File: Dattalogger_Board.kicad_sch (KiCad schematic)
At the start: 25 parts, among them U1 24LC1025, U2 DS1337S_, U3 24LC1025, U4 ATMEGA328P-AU, Y1 32.768 KHz, Y2 16 MHz

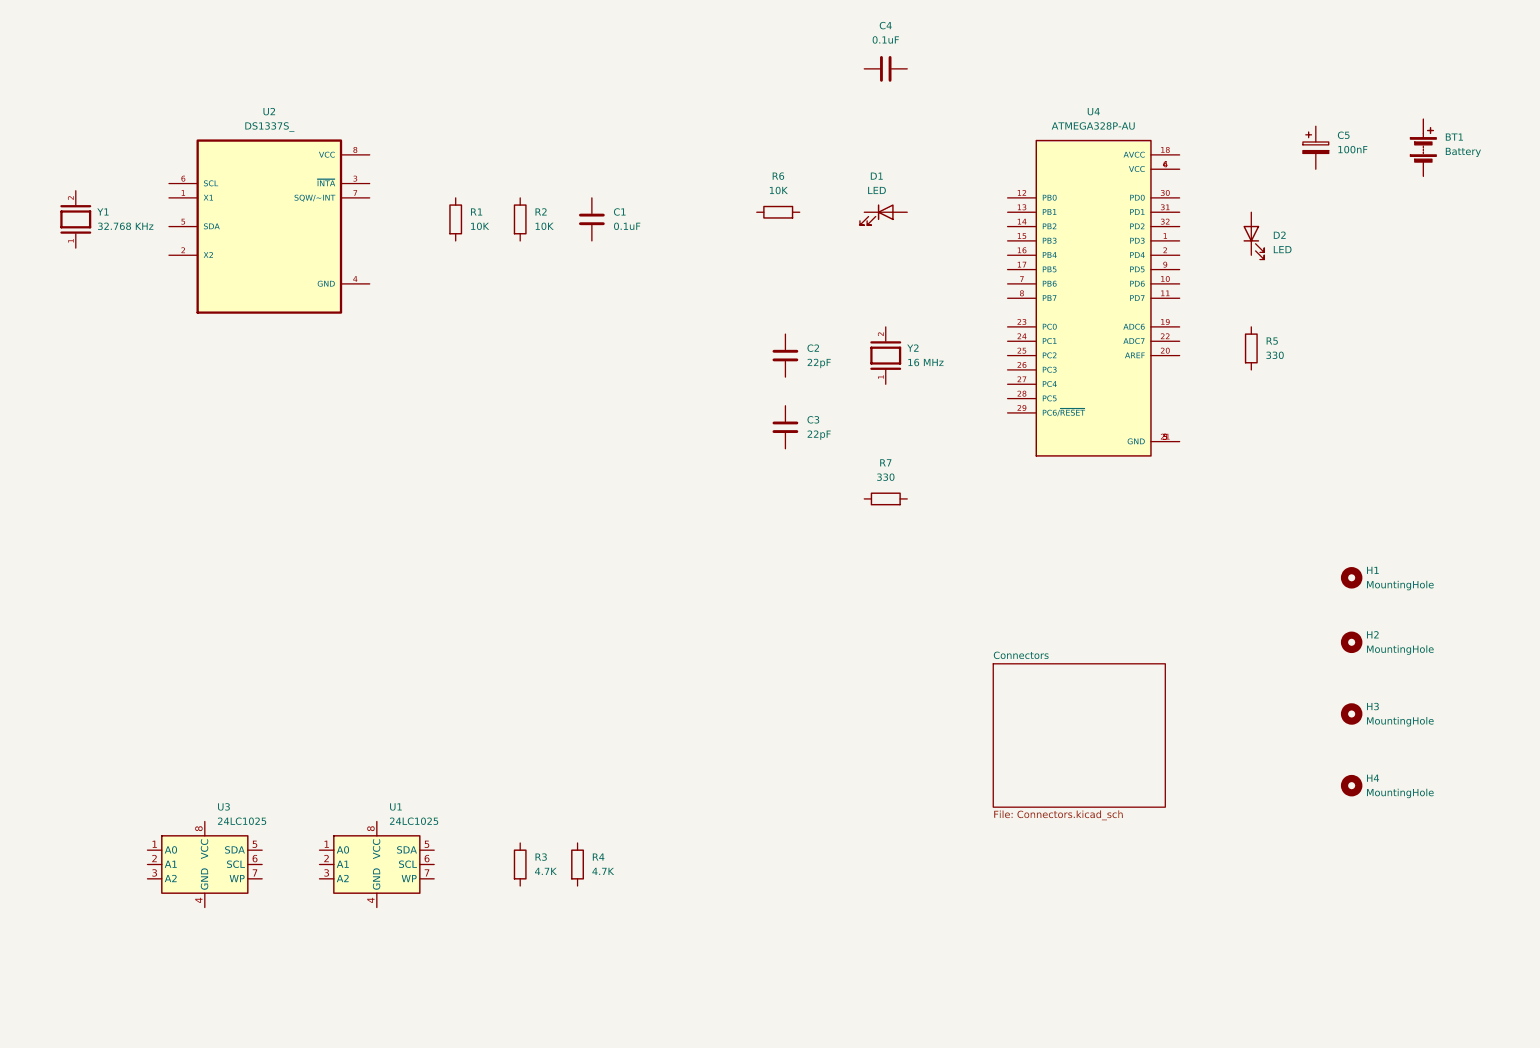
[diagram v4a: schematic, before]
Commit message: The wiring for the root sheet is complete.
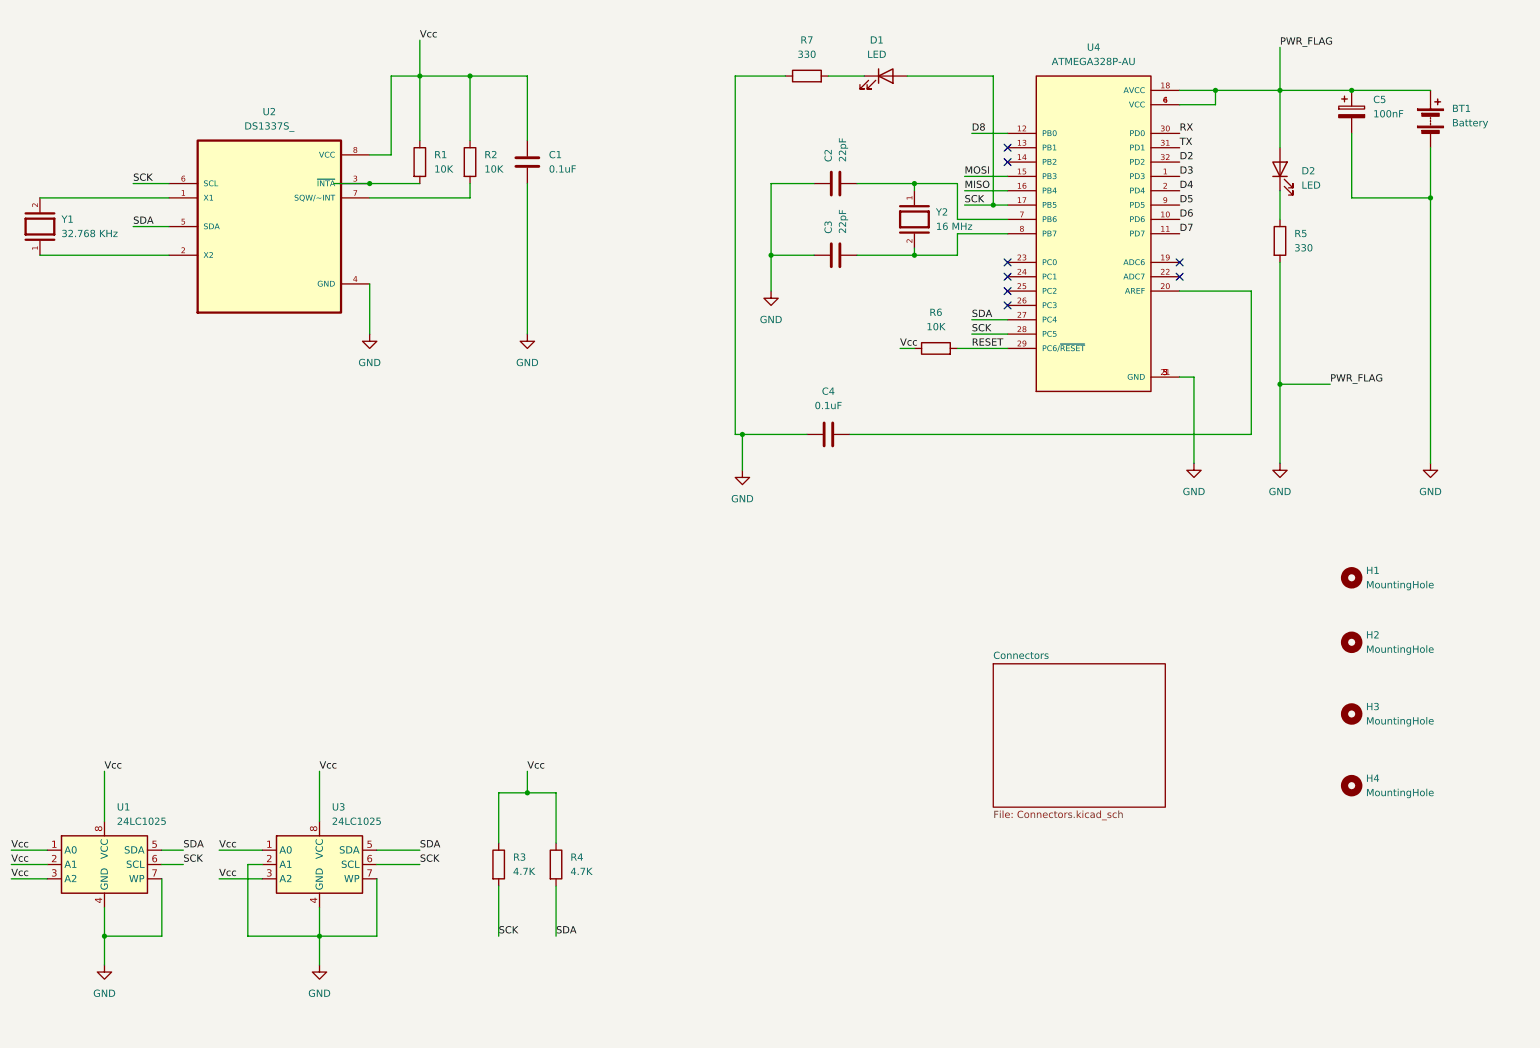
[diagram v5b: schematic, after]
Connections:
- net GND: now reaches C3.1
- net GND: now also BT1.1 (+), BT1.2 (-), C1.2, C2.1, C4.1, C5.1, C5.2, D2.2 (A), R5.2, R7.1, U1.4 (GND), U1.7 (WP), U2.4 (GND), U3.2 (A1), U3.4 (GND), U3.7 (WP), U4.18 (AVCC), U4.21 (GND), U4.3 (GND), U4.4 (VCC), U4.5 (GND), U4.6 (VCC)
- net at C3.2: now also U4.8 (PB7), Y2.2
- net at R7.2: now also D1.1 (K)
- net Vcc: now reaches R6.1
- net Vcc: now also C1.1, R1.1, R2.1, R3.1, R4.1, U1.1 (A0), U1.2 (A1), U1.3 (A2), U1.8 (VCC), U2.8 (VCC), U3.1 (A0), U3.3 (A2), U3.8 (VCC)
- net RESET: now reaches R6.2
- net RESET: now also U4.29 (PC6/~{RESET})
- net at D2.1 (K): now also R5.1
- net at R2.2: now also U2.7 (SQW/~INT)
- net at C4.2: now also U4.20 (AREF)
- net at R1.2: now also U2.3 (~{INTA})
- net SDA: now reaches U3.5 (SDA)
- net SDA: now also R4.2, U1.5 (SDA), U2.5 (SDA), U4.27 (PC4)
- net SCK: now reaches U3.6 (SCL)
- net SCK: now also D1.2 (A), R3.2, U1.6 (SCL), U2.6 (SCL), U4.17 (PB5), U4.28 (PC5)
- net at Y1.1: now also U2.2 (X2)
- net at Y1.2: now also U2.1 (X1)
- net D3: now reaches U4.1 (PD3)
- net D6: now reaches U4.10 (PD6)
- net D7: now reaches U4.11 (PD7)
- net D8: now reaches U4.12 (PB0)
- net MOSI: now reaches U4.15 (PB3)
- net MISO: now reaches U4.16 (PB4)
- net D4: now reaches U4.2 (PD4)
- net RX: now reaches U4.30 (PD0)
- net TX: now reaches U4.31 (PD1)
- net D2: now reaches U4.32 (PD2)
- net at U4.7 (PB6): now also C2.2, Y2.1
- net D5: now reaches U4.9 (PD5)
- no-connect marks 0 -> 8
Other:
- moved on the sheet: BT1, C1, C2, C3, C5, D1, D2, R1, R2, R3, R4, R5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

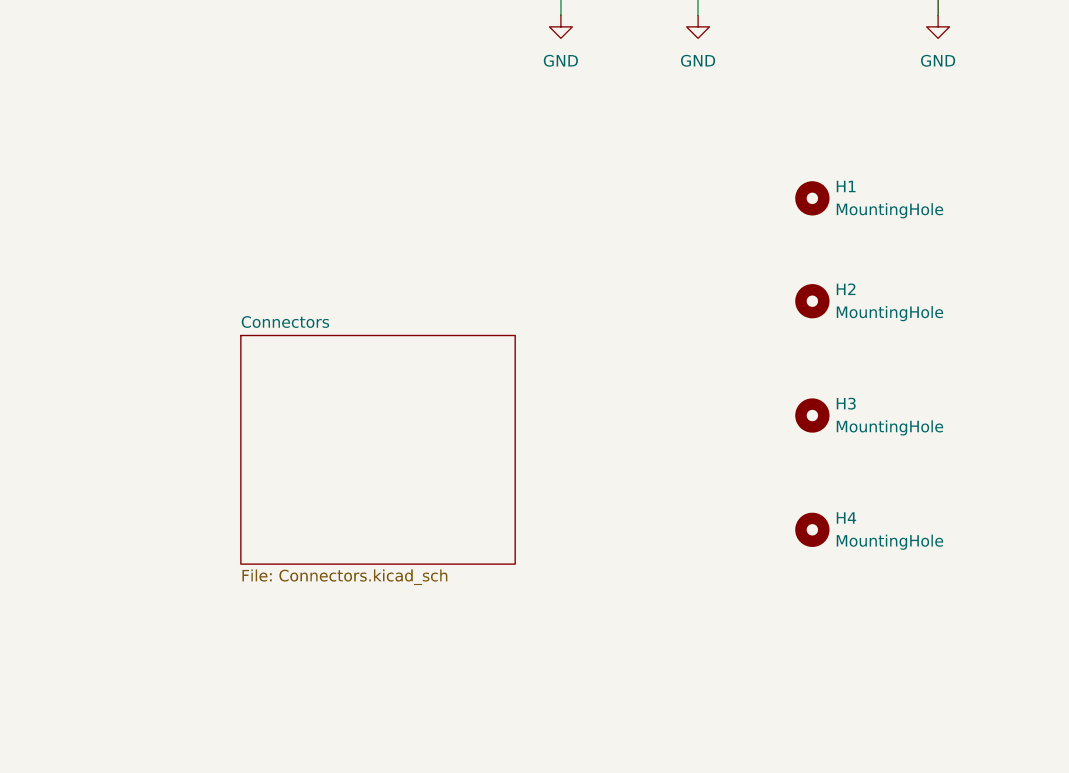
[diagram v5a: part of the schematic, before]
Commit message: Allocated GND and Vcc Nets to the power net class
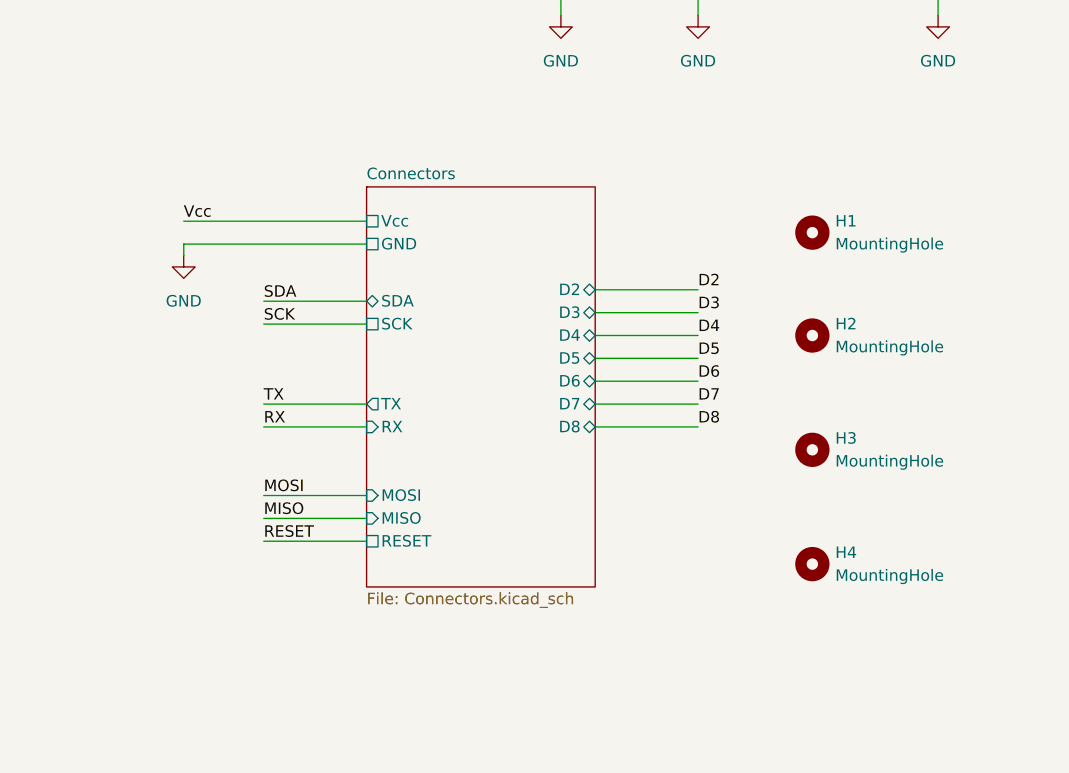
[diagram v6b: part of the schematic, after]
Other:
- sheet Connectors ports: added D2, D3, D4, D5, D6, D7, D8, GND, MISO, MOSI, RESET, RX, SCK, SDA, TX, Vcc; removed none
- moved on the sheet: H1, H2, H3, H4
